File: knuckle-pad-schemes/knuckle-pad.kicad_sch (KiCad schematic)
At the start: 56 parts, among them SW1 SW_Push, SW10 SW_Push, SW11 SW_Push, SW12 SW_Push, SW13 SW_Push, SW14 SW_Push, SW15 SW_Push, SW16 SW_Push, SW17 SW_Push, SW18 SW_Push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

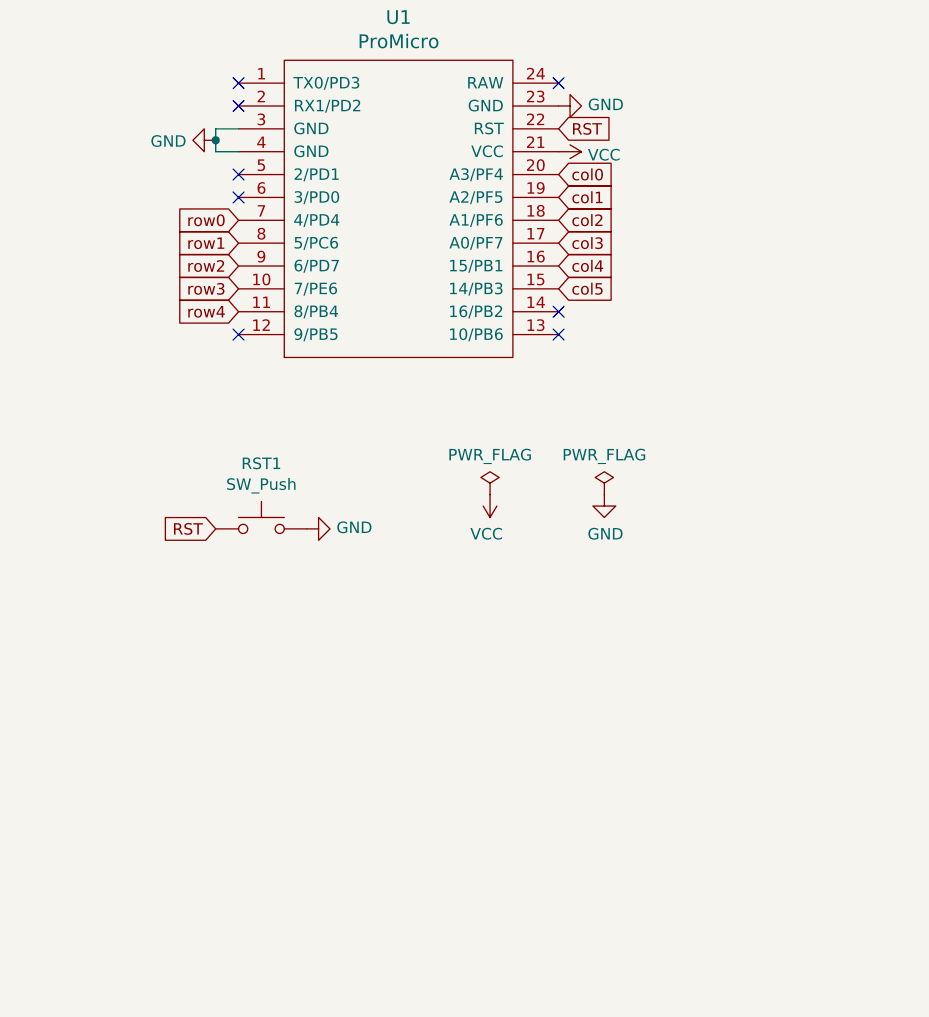
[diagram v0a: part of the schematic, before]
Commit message: moved mcu and switched back to traymount
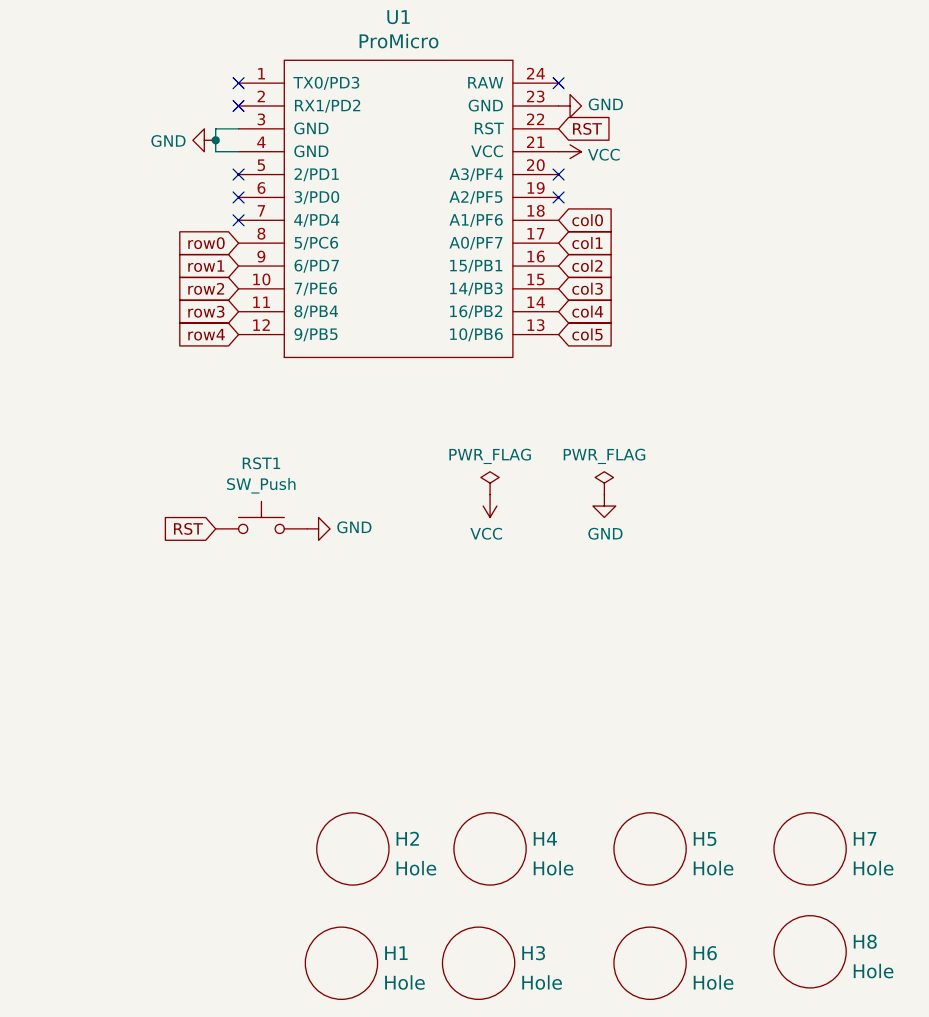
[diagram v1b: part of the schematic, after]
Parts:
- added H1, H2, H3, H4, H5, H6, H7, H8: Hole, used_footprints:M2_HOLE_PCB, symbol keebio:Hole
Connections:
- net col0: now also U1.18 (A1/PF6); no longer U1.20 (A3/PF4)
- net col1: now also U1.17 (A0/PF7); no longer U1.19 (A2/PF5)
- net col2: now also U1.16 (15/PB1); no longer U1.18 (A1/PF6)
- net col3: now also U1.15 (14/PB3); no longer U1.17 (A0/PF7)
- net col4: now also U1.14 (16/PB2); no longer U1.16 (15/PB1)
- net col5: now also U1.13 (10/PB6); no longer U1.15 (14/PB3)
- net row0: now also U1.8 (5/PC6); no longer U1.7 (4/PD4)
- net row1: now also U1.9 (6/PD7); no longer U1.8 (5/PC6)
- net row2: now also U1.10 (7/PE6); no longer U1.9 (6/PD7)
- net row3: now also U1.11 (8/PB4); no longer U1.10 (7/PE6)
- net row4: now also U1.12 (9/PB5); no longer U1.11 (8/PB4)
